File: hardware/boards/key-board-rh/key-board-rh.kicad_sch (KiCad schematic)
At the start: 8 parts, among them J1 12-way

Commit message: Remove the key boards' test pads; SMD pads join the ground pour solid
The owner decided this: a one-off build is probed by hand, so the six
bring-up test pads (TP-CHAIN) come off both key boards. That means their
symbols (with the power symbols and labels stacked on them), the BOM row,
the layout.yaml placements and the silk legend. The bring-up steps now probe
J1's pin tails, with the key-board pin map in the README. carrier.md's
proposed TP-*/LK-* row is marked not fitted, and the main board's open item
is gone.

tools/pcb_route.py pours ground with ZONE_CONNECTION_THT_THERMAL: thermal
spokes on hand-soldered through-hole pads, solid on reflowed SMD pads. Once
the pads were gone, the register's boxed-in ground pin (U1.15) kept tripping
KiCad's starved_thermal.

Key board LH is re-laid out and rendered: 0 check errors, and every net
routes on the first pass. The key-chain simulation and both key boards'
simulations are re-run and pass.

STILL RED: key board RH is not yet re-laid out. That layout search is
running.

Co-Authored-By: Claude Opus 5.5 <noreply@anthropic.com>
Claude-Session: https://claude.ai/code/session_01LmB4muFXnoLprWX4JzuJ5A
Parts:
- removed TP1, TP2, TP3, TP4, TP5, TP6: test pad, TestPoint:TestPoint_Pad_D1.0mm, symbol Connector:TestPoint
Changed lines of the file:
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@@
     (instances (project "key-board-rh" (path "/0d798814-7e94-52b0-a143-b50dd4dde890" (page "8"))))
   )
-  (symbol (lib_id "Connector:TestPoint") (at 27.94 152.4 0) (unit 1)
-    (in_bom no) (on_board yes) (dnp no)
-    (property "Reference" "TP6" (at 27.94 144.78 90) (effects (font (size 1.27 1.27)) (justify left)))
-    (property "Probe" "3V3" (at 0 0 0) (effects (font (size 1.27 1.27)) hide))
-    (property "Value" "test pad" (at 30.48 144.78 90) (effects (font (size 1.27 1.27)) (justify left)))
-    (property "Footprint" "TestPoint:TestPoint_Pad_D1.0mm" (at 27.94 152.4 0) (effects (font (size 1.27 1.27)) hide))
-    (property "Datasheet" "" (at 27.94 152.4 0) (effects (font (size 1.27 1.27)) hide))
-    (property "Row" "TP-CHAIN" (at 27.94 152.4 0) (effects (font (size 1.27 1.27)) hide))
-    (property "Pins" "1=1" (at 27.94 152.4 0) (effects (font (size 1.27 1.27)) hide))
-    (property "Note" "bring-up test pad: the chain's 3V3 at this board (hardware/boards/key-board-rh/README.md)" (at 27.94 152.4 0) (effects (font (size 1.27 1.27)) hide))
-    (property "Assembly" "none" (at 27.94 152.4 0) (effects (font (size 1.27 1.27)) hide))
-    (pin "1")
-    (instances (project "key-board-rh" (path "/0d798814-7e94-52b0-a143-b50dd4dde890" (reference "TP6") (unit 1))))
-  )
-  (symbol (lib_id "power:+3V3") (at 27.94 152.4 0) (unit 1)
-    (in_bom yes) (on_board yes) (dnp no)
-    (property "Reference" "#PWR26" (at 27.94 158.75 0) (effects (font (size 1.27 1.27)) hide))
-    (property "Value" "V3V3_CHAIN_RH" (at 27.94 156.21 0) (effects (font (size 1.27 1.27))))
-    (property "Footprint" "" (at 27.94 152.4 0) (effects (font (size 1.27 1.27)) hide))
-    (property "Datasheet" "" (at 27.94 152.4 0) (effects (font (size 1.27 1.27)) hide))
-    (pin "1")
-    (instances (project "key-board-rh" (path "/0d798814-7e94-52b0-a143-b50dd4dde890" (reference "#PWR26") (unit 1))))
-  )
-  (symbol (lib_id "Connector:TestPoint") (at 38.1 152.4 0) (unit 1)
-    (in_bom no) (on_board yes) (dnp no)
-    (property "Reference" "TP3" (at 38.1 144.78 90) (effects (font (size 1.27 1.27)) (justify left)))
-    (property "Probe" "GND" (at 0 0 0) (effects (font (size 1.27 1.27)) hide))
-    (property "Value" "test pad" (at 40.64 144.78 90) (effects (font (size 1.27 1.27)) (justify left)))
-    (property "Footprint" "TestPoint:TestPoint_Pad_D1.0mm" (at 38.1 152.4 0) (effects (font (size 1.27 1.27)) hide))
-    (property "Datasheet" "" (at 38.1 152.4 0) (effects (font (size 1.27 1.27)) hide))
-    (property "Row" "TP-CHAIN" (at 38.1 152.4 0) (effects (font (size 1.27 1.27)) hide))
-    (property "Pins" "1=1" (at 38.1 152.4 0) (effects (font (size 1.27 1.27)) hide))
-    (property "Note" "bring-up test pad: ground (hardware/boards/key-board-rh/README.md)" (at 38.1 152.4 0) (effects (font (size 1.27 1.27)) hide))
-    (property "Assembly" "none" (at 38.1 152.4 0) (effects (font (size 1.27 1.27)) hide))
-    (pin "1")
-    (instances (project "key-board-rh" (path "/0d798814-7e94-52b0-a143-b50dd4dde890" (reference "TP3") (unit 1))))
-  )
-  (symbol (lib_id "power:GND") (at 38.1 152.4 0) (unit 1)
-    (in_bom yes) (on_board yes) (dnp no)
-    (property "Reference" "#PWR27" (at 38.1 158.75 0) (effects (font (size 1.27 1.27)) hide))
-    (property "Value" "GND_CHAIN" (at 38.1 156.21 0) (effects (font (size 1.27 1.27))))
-    (property "Footprint" "" (at 38.1 152.4 0) (effects (font (size 1.27 1.27)) hide))
-    (property "Datasheet" "" (at 38.1 152.4 0) (effects (font (size 1.27 1.27)) hide))
-    (pin "1")
-    (instances (project "key-board-rh" (path "/0d798814-7e94-52b0-a143-b50dd4dde890" (reference "#PWR27") (unit 1))))
-  )
-  (symbol (lib_id "Connector:TestPoint") (at 48.26 152.4 0) (unit 1)
-    (in_bom no) (on_board yes) (dnp no)
-    (property "Reference" "TP4" (at 48.26 144.78 90) (effects (font (size 1.27 1.27)) (justify left)))
-    (property "Probe" "SCK" (at 0 0 0) (effects (font (size 1.27 1.27)) hide))
-    (property "Value" "test pad" (at 50.8 144.78 90) (effects (font (size 1.27 1.27)) (justify left)))
-    (property "Footprint" "TestPoint:TestPoint_Pad_D1.0mm" (at 48.26 152.4 0) (effects (font (size 1.27 1.27)) hide))
-    (property "Datasheet" "" (at 48.26 152.4 0) (effects (font (size 1.27 1.27)) hide))
-    (property "Row" "TP-CHAIN" (at 48.26 152.4 0) (effects (font (size 1.27 1.27)) hide))
-    (property "Pins" "1=1" (at 48.26 152.4 0) (effects (font (size 1.27 1.27)) hide))
-    (property "Note" "bring-up test pad: the chain's clock (hardware/boards/key-board-rh/README.md)" (at 48.26 152.4 0) (effects (font (size 1.27 1.27)) hide))
-    (property "Assembly" "none" (at 48.26 152.4 0) (effects (font (size 1.27 1.27)) hide))
-    (pin "1")
-    (instances (project "key-board-rh" (path "/0d798814-7e94-52b0-a143-b50dd4dde890" (reference "TP4") (unit 1))))
-  )
-  (label "CHAIN_SCK" (at 48.26 152.4 270) (fields_autoplaced) (effects (font (size 1.27 1.27)) (justify right bottom)))
-  (symbol (lib_id "Connector:TestPoint") (at 58.42 152.4 0) (unit 1)
-    (in_bom no) (on_board yes) (dnp no)
-    (property "Reference" "TP5" (at 58.42 144.78 90) (effects (font (size 1.27 1.27)) (justify left)))
-    (property "Probe" "SH/LD" (at 0 0 0) (effects (font (size 1.27 1.27)) hide))
-    (property "Value" "test pad" (at 60.96 144.78 90) (effects (font (size 1.27 1.27)) (justify left)))
-    (property "Footprint" "TestPoint:TestPoint_Pad_D1.0mm" (at 58.42 152.4 0) (effects (font (size 1.27 1.27)) hide))
-    (property "Datasheet" "" (at 58.42 152.4 0) (effects (font (size 1.27 1.27)) hide))
-    (property "Row" "TP-CHAIN" (at 58.42 152.4 0) (effects (font (size 1.27 1.27)) hide))
-    (property "Pins" "1=1" (at 58.42 152.4 0) (effects (font (size 1.27 1.27)) hide))
-    (property "Note" "bring-up test pad: the chain's shift/load (hardware/boards/key-board-rh/README.md)" (at 58.42 152.4 0) (effects (font (size 1.27 1.27)) hide))
-    (property "Assembly" "none" (at 58.42 152.4 0) (effects (font (size 1.27 1.27)) hide))
-    (pin "1")
-    (instances (project "key-board-rh" (path "/0d798814-7e94-52b0-a143-b50dd4dde890" (reference "TP5") (unit 1))))
-  )
-  (label "CHAIN_SHLD" (at 58.42 152.4 270) (fields_autoplaced) (effects (font (size 1.27 1.27)) (justify right bottom)))
-  (symbol (lib_id "Connector:TestPoint") (at 68.58 152.4 0) (unit 1)
-    (in_bom no) (on_board yes) (dnp no)
-    (property "Reference" "TP1" (at 68.58 144.78 90) (effects (font (size 1.27 1.27)) (justify left)))
-    (property "Probe" "QH" (at 0 0 0) (effects (font (size 1.27 1.27)) hide))
-    (property "Value" "test pad" (at 71.12 144.78 90) (effects (font (size 1.27 1.27)) (justify left)))
-    (property "Footprint" "TestPoint:TestPoint_Pad_D1.0mm" (at 68.58 152.4 0) (effects (font (size 1.27 1.27)) hide))
-    (property "Datasheet" "" (at 68.58 152.4 0) (effects (font (size 1.27 1.27)) hide))
-    (property "Row" "TP-CHAIN" (at 68.58 152.4 0) (effects (font (size 1.27 1.27)) hide))
-    (property "Pins" "1=1" (at 68.58 152.4 0) (effects (font (size 1.27 1.27)) hide))
-    (property "Note" "bring-up test pad: this board's serial output (QH) (hardware/boards/key-board-rh/README.md)" (at 68.58 152.4 0) (effects (font (size 1.27 1.27)) hide))
-    (property "Assembly" "none" (at 68.58 152.4 0) (effects (font (size 1.27 1.27)) hide))
-    (pin "1")
-    (instances (project "key-board-rh" (path "/0d798814-7e94-52b0-a143-b50dd4dde890" (reference "TP1") (unit 1))))
-  )
-  (label "HOP_RH_RT" (at 68.58 152.4 270) (fields_autoplaced) (effects (font (size 1.27 1.27)) (justify right bottom)))
-  (symbol (lib_id "Connector:TestPoint") (at 78.74 152.4 0) (unit 1)
-    (in_bom no) (on_board yes) (dnp no)
-    (property "Reference" "TP2" (at 78.74 144.78 90) (effects (font (size 1.27 1.27)) (justify left)))
-    (property "Probe" "SER" (at 0 0 0) (effects (font (size 1.27 1.27)) hide))
-    (property "Value" "test pad" (at 81.28 144.78 90) (effects (font (size 1.27 1.27)) (justify left)))
-    (property "Footprint" "TestPoint:TestPoint_Pad_D1.0mm" (at 78.74 152.4 0) (effects (font (size 1.27 1.27)) hide))
-    (property "Datasheet" "" (at 78.74 152.4 0) (effects (font (size 1.27 1.27)) hide))
-    (property "Row" "TP-CHAIN" (at 78.74 152.4 0) (effects (font (size 1.27 1.27)) hide))
-    (property "Pins" "1=1" (at 78.74 152.4 0) (effects (font (size 1.27 1.27)) hide))
-    (property "Note" "bring-up test pad: this board's serial input (SER), driven by the next board up the chain - tie it to TP-GND or TP-3V3 on the bench, where nothing drives it (hardware/boards/key-board-rh/README.md)" (at 78.74 152.4 0) (effects (font (size 1.27 1.27)) hide))
-    (property "Assembly" "none" (at 78.74 152.4 0) (effects (font (size 1.27 1.27)) hide))
-    (pin "1")
-    (instances (project "key-board-rh" (path "/0d798814-7e94-52b0-a143-b50dd4dde890" (reference "TP2") (unit 1))))
-  )
-  (label "HOP_LT_RH" (at 78.74 152.4 270) (fields_autoplaced) (effects (font (size 1.27 1.27)) (justify right bottom)))
   (symbol (lib_id "Device:C") (at 93.98 152.4 0) (unit 1)
     (in_bom yes) (on_board yes) (dnp no)

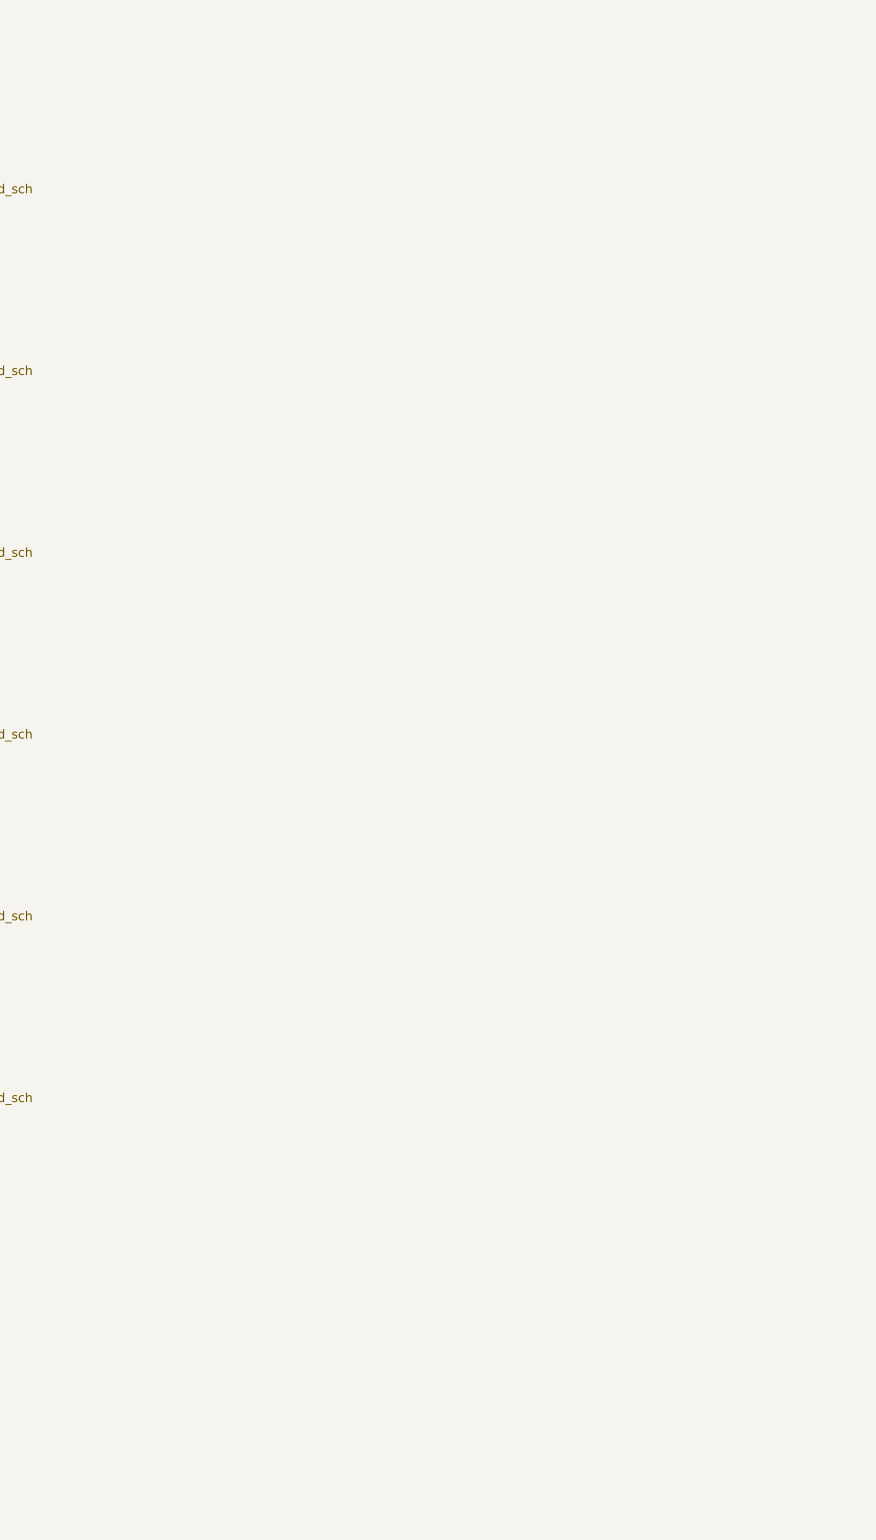
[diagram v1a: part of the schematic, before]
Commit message: Matrix on the right-hand key board (option d): config, body CAD, key board sheet, BOM, nets
Owner, 2026-10-02: 'I think d is right for the matrix vs hand soldering'.
- config/body.yaml: boards.matrix_mount/rail_in/shim_t/support, the IDC
  socket's envelope (mcu_plug_*), openings.usb_plug_turn 'down'; the
  soldered-harness height retired.
- woody_body.scad: the right-hand key board runs on as two rails under the
  Matrix's pad rows; shims; J-MCU-KB above J-MCU and the IDC ribbon's S fold;
  the USB-C plug turned down so its lead passes under the far rail; DRCs.
- key-board-rh sheet: J2 (J-MCU-KB, pin k = J-MCU pin 25-k), J3/J4
  (HDR-MATRIX), J5 (W-MATRIX); the Matrix's grounds on GND_CHAIN. Exported.
- carrier sheet: U-MCU-RT and J-MCU notes follow. Exported and rendered.
- tools/kicad.py: check_matrix holds the key board's Matrix pins to the
  carrier's netlist.
- BOM: CBL-MCU-RIBBON crimped both ends; J-MCU-KB, HDR-MATRIX, W-MATRIX,
  MECH-MATRIX-SHIM; U-ESD-USB not fitted by the owner's decision.
- nets.yaml: GND_CHAIN, EN, IO0, INST_5V_A routes.

CAD outputs other than drc and pcb-geometry are rebuilt in the next commit.

Co-Authored-By: Claude Opus 5.5 <noreply@anthropic.com>
Claude-Session: https://claude.ai/code/session_01LmB4muFXnoLprWX4JzuJ5A
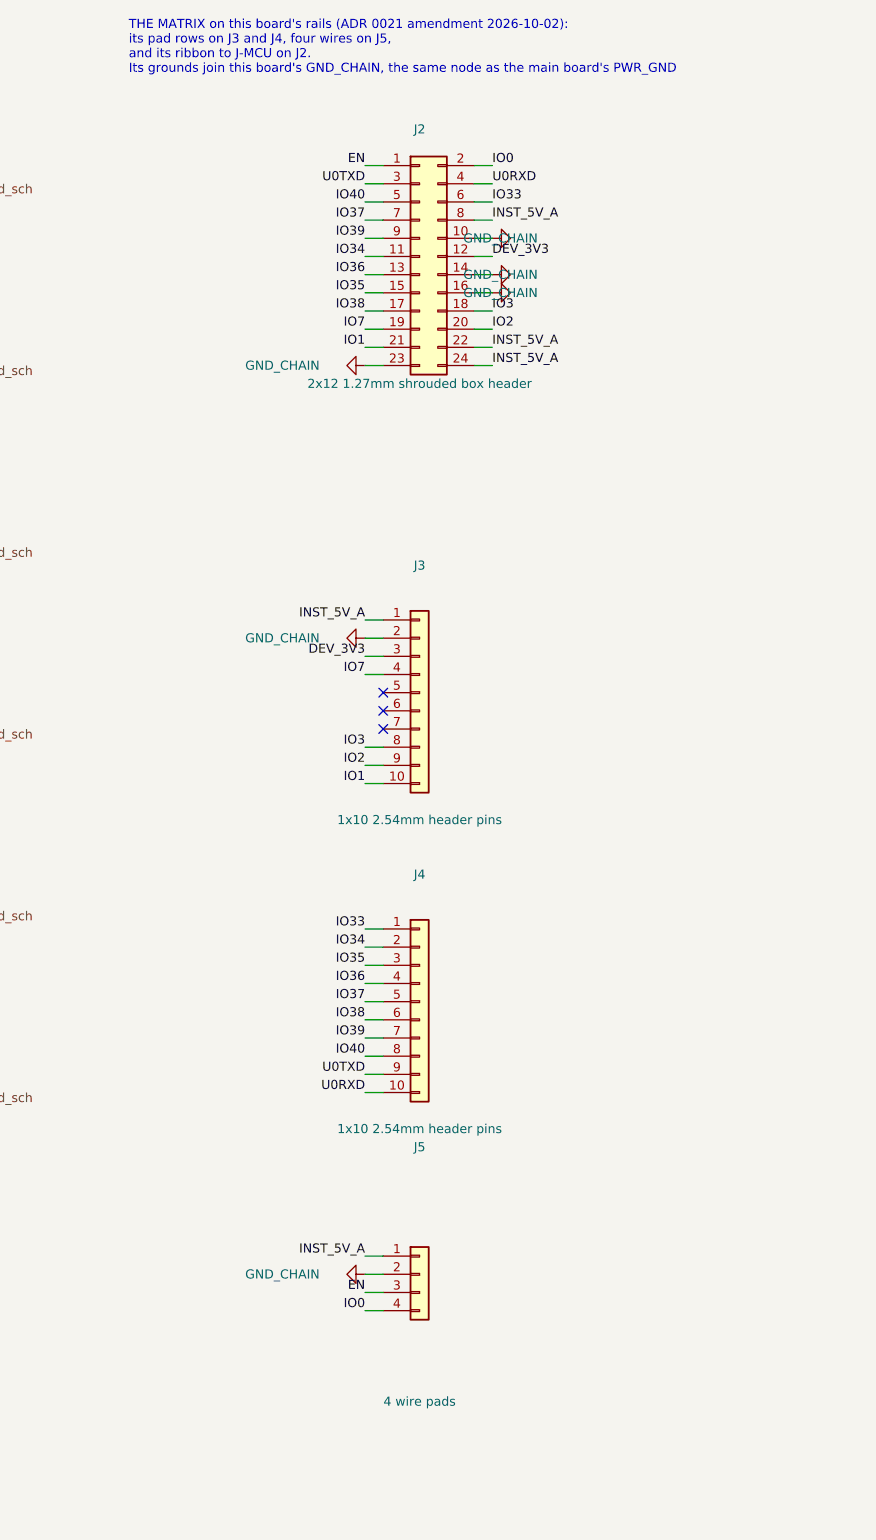
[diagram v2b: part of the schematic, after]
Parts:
- added J2: 2x12 1.27mm shrouded box header, woody:IDC-Header_2x12_P1.27mm_XKB_X1270WR_Horizontal, symbol Connector_Generic:Conn_02x12_Odd_Even
- added J3, J4: 1x10 2.54mm header pins, Connector_PinHeader_2.54mm:PinHeader_1x10_P2.54mm_Vertical, symbol Connector_Generic:Conn_01x10
- added J5: 4 wire pads, Connector_Wire:SolderWire-0.15sqmm_1x04_P4mm_D0.5mm_OD1.5mm, symbol Connector_Generic:Conn_01x04
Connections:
- net GND_CHAIN: now also J2.10 (Pin_10), J2.14 (Pin_14), J2.16 (Pin_16), J2.23 (Pin_23), J3.2 (Pin_2), J5.2 (Pin_2)
- new net DEV_3V3: J2.12 (Pin_12), J3.3 (Pin_3)
- new net EN: J2.1 (Pin_1), J5.3 (Pin_3)
- new net INST_5V_A: J2.22 (Pin_22), J2.24 (Pin_24), J2.8 (Pin_8), J3.1 (Pin_1), J5.1 (Pin_1)
- new net IO0: J2.2 (Pin_2), J5.4 (Pin_4)
- new net IO1: J2.21 (Pin_21), J3.10 (Pin_10)
- new net IO2: J2.20 (Pin_20), J3.9 (Pin_9)
- new net IO3: J2.18 (Pin_18), J3.8 (Pin_8)
- new net IO33: J2.6 (Pin_6), J4.1 (Pin_1)
- new net IO34: J2.11 (Pin_11), J4.2 (Pin_2)
- new net IO35: J2.15 (Pin_15), J4.3 (Pin_3)
- new net IO36: J2.13 (Pin_13), J4.4 (Pin_4)
- new net IO37: J2.7 (Pin_7), J4.5 (Pin_5)
- new net IO38: J2.17 (Pin_17), J4.6 (Pin_6)
- new net IO39: J2.9 (Pin_9), J4.7 (Pin_7)
- new net IO40: J2.5 (Pin_5), J4.8 (Pin_8)
- new net IO7: J2.19 (Pin_19), J3.4 (Pin_4)
- new net U0RXD: J2.4 (Pin_4), J4.10 (Pin_10)
- new net U0TXD: J2.3 (Pin_3), J4.9 (Pin_9)
- no-connect marks 2 -> 5
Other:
- note added: "THE MATRIX on this board's rails (ADR 0021 amendment 2026-10-02): its pad rows on J3 and J4, four wires on J5, and its ribbon to J-MCU on J2. Its grounds join this board's GND_CHAIN, the same node as the main board's PWR_GND"

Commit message: Right-hand key board laid out for the Matrix, its J2 escape drawn by hand; U1's second decoupler at VCC (#23, #6-5, #19 F1)
pcb_route cannot fan out J2 (J-MCU-KB) and Freerouting left connections and no pours, so hardware/boards/key-board-rh/matrix_routes.py runs pcb.py layout with J2-J5's nets held out and their routes kept clear, then draws the Matrix's 24 nets: nested 45-degree fans out of both rows, round the header's ends past the tail columns, along the rails on 0.7 mm lanes, each net dropping to its pin through a via. GND_CHAIN pours on both faces with the router's stitching, the connect_first straps by the router as before, J2's front-row grounds and J3.2 tied to the pours. pcb.py check passes; renders and fab/ re-made.

Review #6-5: the key-register sheet gains C-DECOUPLE-165-VCC (C-DECOUPLE-165 qty 8); here it is C9 at U1 pin 16. The left-hand board (C8) and main board (C205, C206) carry it on their sheets and await their layouts. The rails run 0.5 past the Matrix's tail edge for its last pins' edge clearance (body CAD rebuilding). J5 is a 1x4 2.54 mm pin footprint, the wire pads moved below the lanes; setup-env.sh fetches its and the 1x10's 3D models.

Gate-Red: body CAD outputs rebuilding after the rails' end moved; key-board-lh and main-board .kicad_pcb lack the new decoupler until their layouts (wave 3 / re-layout); main-board .kicad_pcb known stale; breath-adc vdd-ripple known
Co-Authored-By: Claude Opus 5.5 <noreply@anthropic.com>
Claude-Session: https://claude.ai/code/session_01LmB4muFXnoLprWX4JzuJ5A
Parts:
- J5: footprint Connector_Wire:SolderWire-0.15sqmm_1x04_P4mm_D0.5mm_OD1.5mm -> Connector_PinHeader_2.54mm:PinHeader_1x04_P2.54mm_Vertical
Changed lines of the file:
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@@
     (property "Reference" "J5" (at 330.20 185.42 0) (effects (font (size 1.27 1.27))))
     (property "Value" "4 wire pads" (at 330.20 220.98 0) (effects (font (size 1.27 1.27))))
-    (property "Footprint" "Connector_Wire:SolderWire-0.15sqmm_1x04_P4mm_D0.5mm_OD1.5mm" (at 330.20 203.20 0) (effects (font (size 1.27 1.27)) hide))
+    (property "Footprint" "Connector_PinHeader_2.54mm:PinHeader_1x04_P2.54mm_Vertical" (at 330.20 203.20 0) (effects (font (size 1.27 1.27)) hide))
     (property "Datasheet" "" (at 330.20 203.20 0) (effects (font (size 1.27 1.27)) hide))
     (property "Row" "W-MATRIX" (at 330.20 203.20 0) (effects (font (size 1.27 1.27)) hide))
